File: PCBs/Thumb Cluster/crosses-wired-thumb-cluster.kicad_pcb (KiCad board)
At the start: 2 copper layers, 126.8 x 111 mm, 46 parts, among them J1 SM06B-SRSS-TB(LF)(SN), J2 SM06B-SRSS-TB(LF)(SN), J3 Conn_01x02_Socket, J4 Conn_01x14_Pin, J5 Conn_01x14_Pin, J6 Conn_01x02_Socket, P1 TYPE-C-31-M-12 USB, P2 TYPE-C-31-M-12 USB, U1 supermini nrf / nice nano v2, U2 supermini nrf / nice nano v2

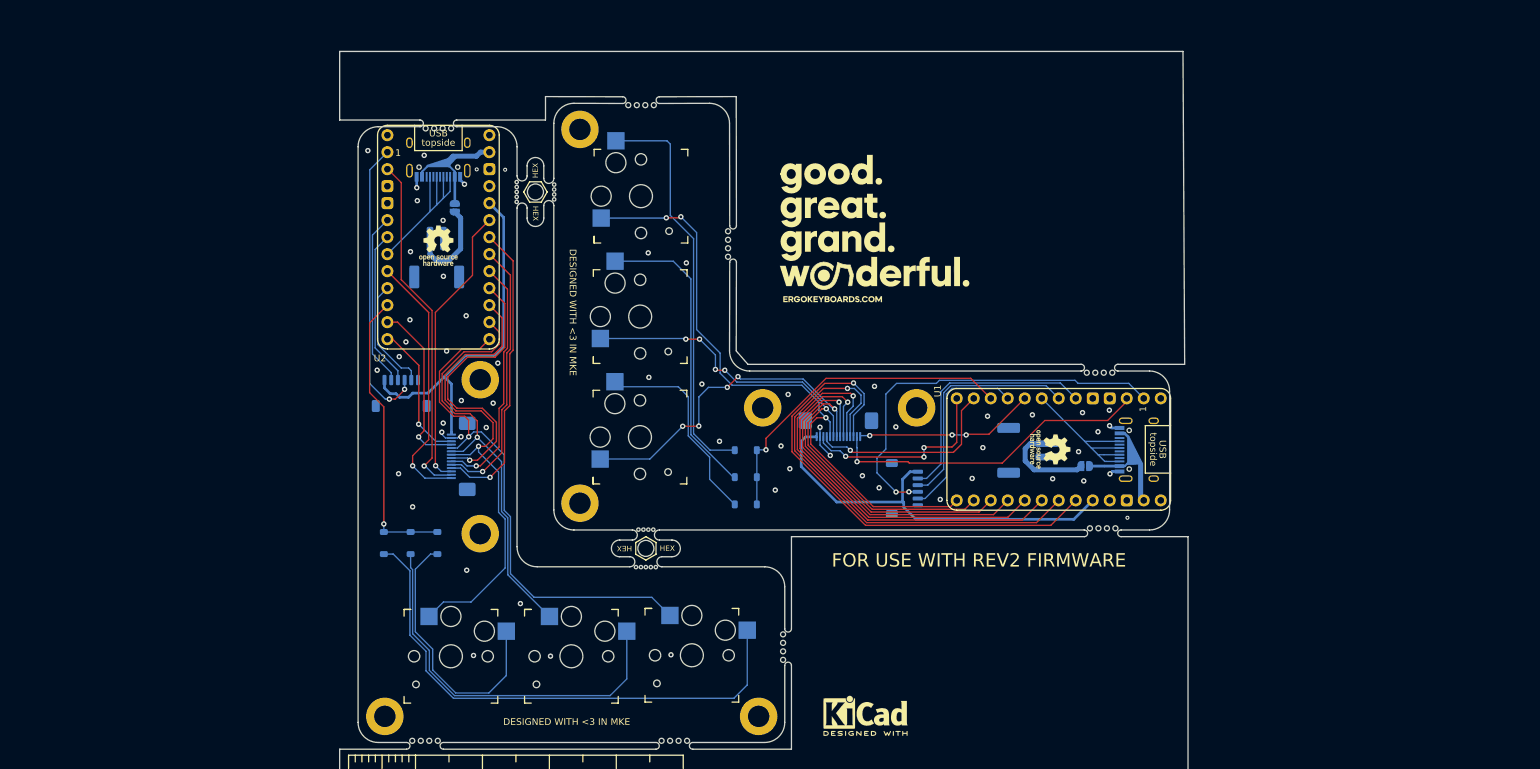
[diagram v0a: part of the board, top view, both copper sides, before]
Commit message: Added a project | Addded a Schematic | Started the board routing
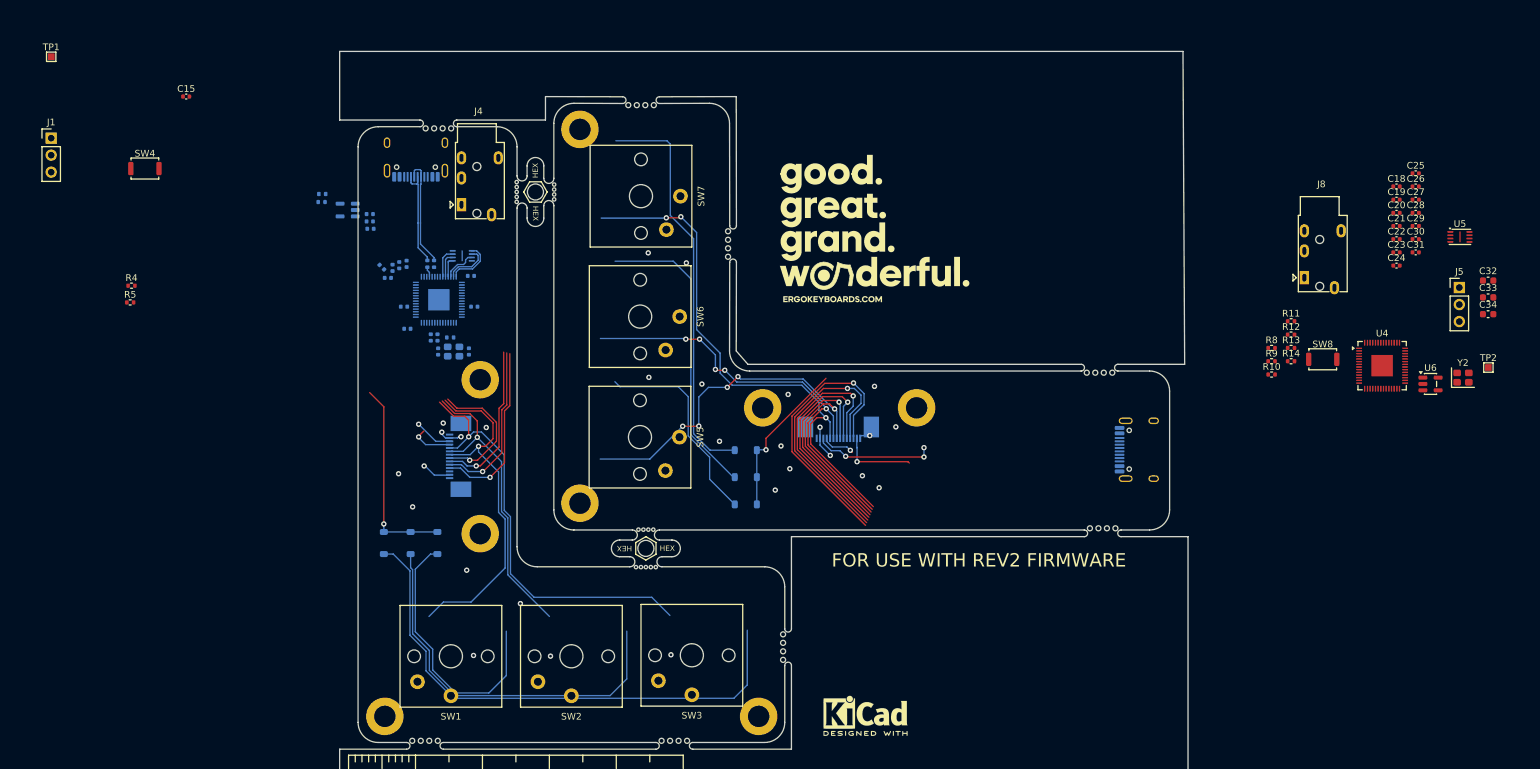
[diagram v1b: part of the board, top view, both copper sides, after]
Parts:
- removed the J2 at (106.7, 147.6)
- removed the J3 at (200.3, 156.1)
- removed the J6 at (112.0, 127.3)
- removed JP1, JP2: SolderJumper_2_Open, Jumper:SolderJumper-2_P1.3mm_Open_RoundedPad1.0x1.5mm
- removed the REF** at (112.2, 125.5)
- removed the REF** at (203.7, 156.0)
- added C1: 15pF, Capacitor_SMD:C_0402_1005Metric, B.Cu at (116.8, 141.3)
- added C10: 0.1uF, Capacitor_SMD:C_0402_1005Metric, B.Cu at (105.4, 128.8)
- added C11: 0.1uF, Capacitor_SMD:C_0402_1005Metric, B.Cu at (104.7, 130.3)
- added C12: 0.1uF, Capacitor_SMD:C_0402_1005Metric, B.Cu at (117.1, 130.0)
- added C13: 0.1uF, Capacitor_SMD:C_0402_1005Metric, B.Cu at (111.1, 139.2)
- added C14: 0.1uF, Capacitor_SMD:C_0402_1005Metric, B.Cu at (107.5, 128.2)
- added C15: 1uF, Capacitor_SMD:C_0402_1005Metric, F.Cu at (74.6, 103.2)
- added C16: 1uF, Capacitor_SMD:C_0402_1005Metric, B.Cu at (102.0, 120.8)
- added C17: 1uF, Capacitor_SMD:C_0402_1005Metric, B.Cu at (102.0, 121.9)
- added C18: 15pF, Capacitor_SMD:C_0402_1005Metric, F.Cu at (255.4, 116.7)
- added C19: 1uF, Capacitor_SMD:C_0402_1005Metric, F.Cu at (255.4, 118.7)
- added C2: 1uF, Capacitor_SMD:C_0402_1005Metric, B.Cu at (102.1, 123.0)
- added C20: 1uF, Capacitor_SMD:C_0402_1005Metric, F.Cu at (255.4, 120.6)
- added C21: 15pF, Capacitor_SMD:C_0402_1005Metric, F.Cu at (255.4, 122.6)
- added C22: 0.1uF, Capacitor_SMD:C_0402_1005Metric, F.Cu at (255.4, 124.6)
- added C23: 0.1uF, Capacitor_SMD:C_0402_1005Metric, F.Cu at (255.4, 126.5)
- added C24: 0.1uF, Capacitor_SMD:C_0402_1005Metric, F.Cu at (255.4, 128.5)
- added C25: 0.1uF, Capacitor_SMD:C_0402_1005Metric, F.Cu at (258.3, 114.7)
- added C26: 0.1uF, Capacitor_SMD:C_0402_1005Metric, F.Cu at (258.3, 116.7)
- added C27: 0.1uF, Capacitor_SMD:C_0402_1005Metric, F.Cu at (258.3, 118.7)
- added C28: 0.1uF, Capacitor_SMD:C_0402_1005Metric, F.Cu at (258.3, 120.6)
- added C29: 0.1uF, Capacitor_SMD:C_0402_1005Metric, F.Cu at (258.3, 122.6)
- added C3: 1uF, Capacitor_SMD:C_0402_1005Metric, B.Cu at (107.6, 137.9)
- added C30: 0.1uF, Capacitor_SMD:C_0402_1005Metric, F.Cu at (258.3, 124.6)
- added C31: 0.1uF, Capacitor_SMD:C_0402_1005Metric, F.Cu at (258.3, 126.5)
- added C32: 1uF, Capacitor_SMD:C_0603_1608Metric, F.Cu at (269.1, 130.7)
- added C33: 1uF, Capacitor_SMD:C_0603_1608Metric, F.Cu at (269.1, 133.2)
- added C34: 1uF, Capacitor_SMD:C_0603_1608Metric, F.Cu at (269.1, 135.8)
- added C4: 15pF, Capacitor_SMD:C_0402_1005Metric, B.Cu at (112.2, 141.3)
- added C5: 0.1uF, Capacitor_SMD:C_0402_1005Metric, B.Cu at (117.6, 134.6)
- added C6: 0.1uF, Capacitor_SMD:C_0402_1005Metric, B.Cu at (107.1, 134.6)
- added C7: 0.1uF, Capacitor_SMD:C_0402_1005Metric, B.Cu at (103.8, 128.7)
- added C8: 0.1uF, Capacitor_SMD:C_0402_1005Metric, B.Cu at (112.1, 139.2)
- added C9: 0.1uF, Capacitor_SMD:C_0402_1005Metric, B.Cu at (106.4, 128.4)
- added J4: AudioJack4, Connector_Audio:Jack_3.5mm_PJ320E_Horizontal, F.Cu at (115.7, 119.4)
- added J5: Conn_01x03, Connector_PinHeader_2.54mm:PinHeader_1x03_P2.54mm_Vertical, F.Cu at (264.8, 131.8)
- added J8: AudioJack4, Connector_Audio:Jack_3.5mm_PJ320E_Horizontal, F.Cu at (241.6, 130.3)
- added R1: 1K, Resistor_SMD:R_0402_1005Metric, B.Cu at (114.0, 139.2)
- added R10: 27, Resistor_SMD:R_0402_1005Metric, F.Cu at (236.7, 144.8)
- added R11: 1K, Resistor_SMD:R_0402_1005Metric, F.Cu at (239.7, 136.8)
- added R12: 10K, Resistor_SMD:R_0402_1005Metric, F.Cu at (239.7, 138.8)
- added R13: 5.1K, Resistor_SMD:R_0402_1005Metric, F.Cu at (239.7, 140.8)
- added R14: 5.1K, Resistor_SMD:R_0402_1005Metric, F.Cu at (239.7, 142.8)
- added R2: 27, Resistor_SMD:R_0402_1005Metric, B.Cu at (110.6, 128.2)
- added R3: 27, Resistor_SMD:R_0402_1005Metric, B.Cu at (111.6, 128.2)
- added R4: 1K, Resistor_SMD:R_0402_1005Metric, F.Cu at (66.4, 131.5)
- added R5: 10K, Resistor_SMD:R_0402_1005Metric, F.Cu at (66.2, 134.0)
- added R6: 5.1K, Resistor_SMD:R_0402_1005Metric, B.Cu at (94.9, 117.8)
- added R7: 5.1K, Resistor_SMD:R_0402_1005Metric, B.Cu at (94.8, 119.0)
- added R8: 1K, Resistor_SMD:R_0402_1005Metric, F.Cu at (236.7, 140.8)
- added R9: 27, Resistor_SMD:R_0402_1005Metric, F.Cu at (236.7, 142.8)
- added SW4: SW_Push, Button_Switch_SMD:SW_Push_SPST_NO_Alps_SKRK, F.Cu at (68.4, 114.0)
- added SW8: SW_Push, Button_Switch_SMD:SW_Push_SPST_NO_Alps_SKRK, F.Cu at (244.4, 142.5)
- added TP1: TestPoint, TestPoint:TestPoint_Pad_1.0x1.0mm, F.Cu at (54.4, 97.3)
- added TP2: TestPoint, TestPoint:TestPoint_Pad_1.0x1.0mm, F.Cu at (269.1, 143.7)
- added U3: XC6210B332MR, Package_TO_SOT_SMD:SOT-23-5, B.Cu at (98.7, 120.2)
- added U4: RP2040, Package_DFN_QFN:QFN-56-1EP_7x7mm_P0.4mm_EP3.2x3.2mm, F.Cu at (253.3, 143.4)
- added U5: W25Q128JVS, Package_SON:Winbond_USON-8-1EP_3x2mm_P0.5mm_EP0.2x1.6mm, F.Cu at (264.9, 124.2)
- added U6: XC6210B332MR, Package_TO_SOT_SMD:SOT-23-5, F.Cu at (260.5, 146.2)
- added Y1: Crystal_GND24, Crystal:Crystal_SMD_2520-4Pin_2.5x2.0mm, B.Cu at (114.5, 141.3)
- added Y2: Crystal_GND24, Crystal:Crystal_SMD_2520-4Pin_2.5x2.0mm, F.Cu at (265.3, 145.2)
- D1: renamed from D6; value 1N4148 -> D
- D2: renamed from D5; value 1N4148 -> D
- D3: renamed from D4; value 1N4148 -> D
- D4: renamed from D1; value 1N4148 -> D
- D5: renamed from D2; value 1N4148 -> D
- D6: renamed from D3; value 1N4148 -> D
- J1: value SM06B-SRSS-TB(LF)(SN) -> Conn_01x03; footprint Connector_JST:JST_SH_SM06B-SRSS-TB_1x06-1MP_P1.00mm_Horizontal -> Connector_PinHeader_2.54mm:PinHeader_1x03_P2.54mm_Vertical; moved to F.Cu
- J2: renamed from P2; value TYPE-C-31-M-12 USB -> USB_C_Receptacle_USB2.0_16P; footprint PCM_marbastlib-various:USB_C_Receptacle_HRO_TYPE-C-31-M-12 -> Connector_USB:USB_C_Receptacle_HRO_TYPE-C-31-M-12
- J3: renamed from J5; footprint PCM_marbastlib-various:XUNPU_FPC-05F-14PH20_1x14-1MP_P0.5mm_Horizontal -> Connector_FFC-FPC:TE_1-1734839-4_1x14-1MP_P0.5mm_Horizontal
- J6: renamed from P1; value TYPE-C-31-M-12 USB -> USB_C_Receptacle_USB2.0_16P; footprint PCM_marbastlib-various:USB_C_Receptacle_HRO_TYPE-C-31-M-12 -> Connector_USB:USB_C_Receptacle_HRO_TYPE-C-31-M-12
- J7: renamed from J4; footprint PCM_marbastlib-various:XUNPU_FPC-05F-14PH20_1x14-1MP_P0.5mm_Horizontal -> Connector_FFC-FPC:TE_1-1734839-4_1x14-1MP_P0.5mm_Horizontal
- SW1: renamed from CH6; value CPG135001S30 -> SW_Push; footprint keyswitches:Kailh_socket_PG1350 -> PCM_Switch_Keyboard_Kailh:SW_Kailh_Choc_V1_1.00u
- SW2: renamed from CH5; value CPG135001S30 -> SW_Push; footprint keyswitches:Kailh_socket_PG1350 -> PCM_Switch_Keyboard_Kailh:SW_Kailh_Choc_V1_1.00u
- SW3: renamed from CH4; value CPG135001S30 -> SW_Push; footprint keyswitches:Kailh_socket_PG1350 -> PCM_Switch_Keyboard_Kailh:SW_Kailh_Choc_V1_1.00u
- SW5: renamed from CH3; value CPG135001S30 -> SW_Push; footprint keyswitches:Kailh_socket_PG1350 -> PCM_Switch_Keyboard_Kailh:SW_Kailh_Choc_V1_1.00u
- SW6: renamed from CH2; value CPG135001S30 -> SW_Push; footprint keyswitches:Kailh_socket_PG1350 -> PCM_Switch_Keyboard_Kailh:SW_Kailh_Choc_V1_1.00u
- SW7: renamed from CH1; value CPG135001S30 -> SW_Push; footprint keyswitches:Kailh_socket_PG1350 -> PCM_Switch_Keyboard_Kailh:SW_Kailh_Choc_V1_1.00u
- U1: value supermini nrf / nice nano v2 -> RP2040; footprint PCM_marbastlib-xp-promicroish:Helios_AH_USBup -> Package_DFN_QFN:QFN-56-1EP_7x7mm_P0.4mm_EP3.2x3.2mm; moved to B.Cu
- U2: value supermini nrf / nice nano v2 -> W25Q128JVS; footprint PCM_marbastlib-xp-promicroish:Helios_AH_USBup -> Package_SON:Winbond_USON-8-1EP_3x2mm_P0.5mm_EP0.2x1.6mm; moved to B.Cu
- moved J1 137.8 mm to (54.4, 109.5), turned to 0 degrees
- moved U1 94.1 mm to (112.3, 133.6), turned to 180 degrees
- moved U2 3.87 mm to (115.8, 127.0), turned to 180 degrees
- moved J2 3.35 mm to (108.9, 111.2)
- renumbered H3 to H1, H3 to H2, H2 to H3, H1 to H4, H3 to H5, H3 to H6, H2 to H7, H1 to H8
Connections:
- D1 pad 1: R-ROW3 -> /R-ROW3
- D2 pad 1: R-ROW3 -> /R-ROW3
- D3 pad 1: R-ROW3 -> /R-ROW3
- D4 pad 1: L-ROW3 -> /L-ROW3
- D4 pad 2: Net-(D1-A) (its old number) -> Net-(D4-A)
- D5 pad 1: L-ROW3 -> /L-ROW3
- D6 pad 1: L-ROW3 -> /L-ROW3
- D6 pad 2: Net-(D3-A) (its old number) -> Net-(D6-A)
- J1 pad 1: GND -> /R-SWCLK
- J1 pad 2: L-CS -> GND-R
- J1 pad 3: L-MISO -> /R-SWDI0
- J2 pad A1: GND -> GND-R
- J2 pad A12: GND -> GND-R
- J2 pad A4: VBATTR -> VBUS-R
- J2 pad A5: R-DATA -> Net-(J2-CC1)
- J2 pad A6: R-DATA -> /R-USB_DP
- J2 pad A7: unconnected-(P2-D--PadA7) -> /R-USB_DN
- J2 pad A8: (no net) -> unconnected-(J2-SBU1-PadA8)
- J2 pad A9: VBATTR -> VBUS-R
- J2 pad B1: GND -> GND-R
- J2 pad B12: GND -> GND-R
- J2 pad B4: VBATTR -> VBUS-R
- J2 pad B5: R-DATA -> Net-(J2-CC2)
- J2 pad B6: R-DATA -> /R-USB_DP
- J2 pad B7: unconnected-(P2-D--PadB7) -> /R-USB_DN
- J2 pad B8: (no net) -> unconnected-(J2-SBU2-PadB8)
- J2 pad B9: VBATTR -> VBUS-R
- J3 pad 1: R-VCC -> unconnected-(J3-Pin_1-Pad1)
- J3 pad 10: R-ROW0 -> /R-ROW0
- J3 pad 11: R-ROW1 -> /R-ROW1
- J3 pad 12: R-ROW2 -> /R-ROW2
- J3 pad 13: R-COLP -> /R-COLP
- J3 pad 14: R-ROWH -> /R-ROWH
- J3 pad 2: GND -> GND-R
- J3 pad 3: R-I2C SCL -> unconnected-(J3-Pin_3-Pad3)
- J3 pad 4: R-I2C SDA -> unconnected-(J3-Pin_4-Pad4)
- J3 pad 5: R-COL2 -> /R-COL2
- J3 pad 6: R-COL3 -> /R-COL3
- J3 pad 7: R-COL4 -> /R-COL4
- J3 pad 8: R-COL1 -> /R-COL1
- J3 pad 9: R-COL0 -> /R-COL0
- J6 pad A1: GND -> GND-L
- J6 pad A12: GND -> GND-L
- J6 pad A4: VBATTL -> VBUS-L
- J6 pad A5: L-DATA -> Net-(J6-CC1)
- J6 pad A6: L-DATA -> /L-USB_DP
- J6 pad A7: unconnected-(P1-D--PadA7) -> /L-USB_DM
- J6 pad A8: (no net) -> unconnected-(J6-SBU1-PadA8)
- J6 pad A9: VBATTL -> VBUS-L
- J6 pad B1: GND -> GND-L
- J6 pad B12: GND -> GND-L
- J6 pad B4: VBATTL -> VBUS-L
- J6 pad B5: L-DATA -> Net-(J6-CC2)
- J6 pad B6: L-DATA -> /L-USB_DP
- J6 pad B7: unconnected-(P1-D--PadB7) -> /L-USB_DM
- J6 pad B8: (no net) -> unconnected-(J6-SBU2-PadB8)
- J6 pad B9: VBATTL -> VBUS-L
- J7 pad 1: L-VCC -> unconnected-(J7-Pin_1-Pad1)
- J7 pad 10: L-ROW0 -> /L-ROW0
- J7 pad 11: L-ROW1 -> /L-ROW1
- J7 pad 12: L-ROW2 -> /L-ROW2
- J7 pad 13: L-COLP -> /L-COLP
- J7 pad 14: L-ROWH -> /L-ROWH
- J7 pad 2: GND -> GND-L
- J7 pad 3: L-I2C SCL -> unconnected-(J7-Pin_3-Pad3)
- J7 pad 4: L-I2C SDA -> unconnected-(J7-Pin_4-Pad4)
- J7 pad 5: L-COL2 -> /L-COL2
- J7 pad 6: L-COL3 -> /L-COL3
- J7 pad 7: L-COL4 -> /L-COL4
- J7 pad 8: L-COL1 -> /L-COL1
- J7 pad 9: L-COL0 -> /L-COL0
- SW1 pad 1: R-COL4 -> /R-COL4
- SW2 pad 1: R-COL3 -> /R-COL3
- SW3 pad 1: R-COL2 -> /R-COL2
- SW5 pad 1: L-COL4 -> /L-COL4
- SW5 pad 2: Net-(D3-A) (its old number) -> Net-(D4-A)
- SW6 pad 1: L-COL3 -> /L-COL3
- SW7 pad 1: L-COL2 -> /L-COL2
- SW7 pad 2: Net-(D1-A) (its old number) -> Net-(D6-A)
- U1 pad 1: L-MISO -> +3V3-R
- U1 pad 10: L-ROW3 -> +3V3-R
- U1 pad 11: L-I2C SDA -> unconnected-(U1-GPIO8-Pad11)
- U1 pad 12: L-I2C SCL -> unconnected-(U1-GPIO9-Pad12)
- U1 pad 13: VBATTL -> unconnected-(U1-GPIO10-Pad13)
- U1 pad 14: GND -> unconnected-(U1-GPIO11-Pad14)
- U1 pad 16: L-VCC -> unconnected-(U1-GPIO13-Pad16)
- U1 pad 17: L-ROW2 -> unconnected-(U1-GPIO14-Pad17)
- U1 pad 18: L-ROW1 -> unconnected-(U1-GPIO15-Pad18)
- U1 pad 19: L-ROW0 -> GND-R
- U1 pad 2: L-COLP -> unconnected-(U1-GPIO0-Pad2)
- U1 pad 20: L-COL0 -> Net-(U1-XIN)
- U1 pad 21: L-COL1 -> Net-(U1-XOUT)
- U1 pad 22: L-COL4 -> +3V3-R
- U1 pad 23: L-COL3 -> +1V1-R
- U1 pad 24: L-COL2 -> /R-SWCLK
- U1 pad 3: GND -> unconnected-(U1-GPIO1-Pad3)
- U1 pad 31: (no net) -> unconnected-(U1-GPIO20-Pad31)
- U1 pad 4: GND -> unconnected-(U1-GPIO2-Pad4)
- U1 pad 5: L-SCK -> unconnected-(U1-GPIO3-Pad5)
- U1 pad 6: L-MOSI -> unconnected-(U1-GPIO4-Pad6)
- U1 pad 7: L-DATA -> unconnected-(U1-GPIO5-Pad7)
- U1 pad 8: L-ROWH -> unconnected-(U1-GPIO6-Pad8)
- U1 pad 9: L-CS -> unconnected-(U1-GPIO7-Pad9)
- U2 pad 1: R-MISO -> /R-QSPI_SS
- U2 pad 2: R-COLP -> /R-QSPI_SD1
- U2 pad 3: GND -> /R-QSPI_SD2
- U2 pad 4: GND -> GND-R
- U2 pad 5: R-SCK -> /R-QSPI_SD0
- U2 pad 6: R-MOSI -> /R-QSPI_SCLK
- U2 pad 7: R-DATA -> /R-QSPI_SD3
- U2 pad 8: R-ROWH -> +3V3-R
- U2 pad 9: R-CS -> (no net)
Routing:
- net Net-(D4-A): track 0.00 -> 139.8 mm
- net L-COL2: track 91.9 -> 0.00 mm, vias 3 -> 0
- net L-COL4: track 90.9 -> 0.00 mm, vias 5 -> 0
- net L-COL3: track 80.4 -> 0.00 mm, vias 5 -> 0
- net Net-(D3-A): track 79.6 -> 0.00 mm
- net /L-COL2: track 0.00 -> 79.0 mm, vias 0 -> 3
- net R-COL2: track 76.9 -> 0.00 mm, vias 1 -> 0
- net L-ROW2: track 74.4 -> 0.00 mm, vias 1 -> 0
- net R-COL4: track 73.3 -> 0.00 mm, vias 1 -> 0
- net /L-COL4: track 0.00 -> 72.3 mm, vias 0 -> 5
- net Net-(D6-A): track 0.00 -> 71.3 mm
- net L-ROW1: track 69.3 -> 0.00 mm, vias 1 -> 0
- net /L-COL3: track 0.00 -> 64.7 mm, vias 0 -> 5
- net L-ROW0: track 63.3 -> 0.00 mm, vias 1 -> 0
- net R-COL3: track 63.3 -> 0.00 mm, vias 1 -> 0
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- added copper zone on B.Cu, net GND-L
- added copper zone on F.Cu, net GND-L
- removed copper zone on B.Cu, net GND
- removed copper zone on F.Cu, net GND
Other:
- copper layers 2 -> 4
- board text removed: "CROSSES REV12"
- board text removed: "DESIGNED WITH <3 IN MKE"

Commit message: Finished routing right side thumb cluster
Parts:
- removed REF** (x8): mousebites 1mm, PCM_marbastlib-various:mousebites_1mm
- removed REF**: KiCad-Logo2_5mm_SilkScreen, Symbol:KiCad-Logo2_5mm_SilkScreen
- removed REF**: Gauge_50mm_Type1_SilkScreenTop, Calibration_Scale:Gauge_50mm_Type1_SilkScreenTop
- C15, R4, R5, TP1: moved to B.Cu
- C2, C3: footprint Capacitor_SMD:C_0402_1005Metric -> Capacitor_SMD:C_0603_1608Metric
- moved TP1 165.3 mm to (214.3, 139.4)
- moved SW4 164.5 mm to (232.7, 122.4), turned to -90 degrees
- moved R5 164.1 mm to (230.2, 127.7), turned to 90 degrees
- moved R4 163.9 mm to (230.2, 125.7), turned to -90 degrees
- moved J1 163.7 mm to (213.5, 148.1), turned to 180 degrees
- moved C15 152.9 mm to (225.8, 125.8)
- moved R7 133.3 mm to (228.1, 117.5), turned to 90 degrees
- moved R6 130.2 mm to (225.1, 117.5), turned to -90 degrees
- moved U3 124.3 mm to (223.0, 120.5), turned to -90 degrees
- moved C17 119.5 mm to (221.5, 123.2)
- moved C16 118.8 mm to (220.8, 120.6), turned to -90 degrees
- moved J2 117.5 mm to (226.4, 111.2)
- moved C2 114.4 mm to (216.4, 128.9), turned to 90 degrees
- moved C7 114.1 mm to (217.9, 127.4)
- moved C11 113.3 mm to (218.0, 130.9)
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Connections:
- R2 pad 2: Net-(U1-USB_DM) -> /R-USB_DN
- R3 pad 1: Net-(U1-USB_DP) -> /R-USB_DP
- U1 pad 12: unconnected-(U1-GPIO9-Pad12) -> /R-ROW1
- U1 pad 13: unconnected-(U1-GPIO10-Pad13) -> /R-ROW0
- U1 pad 14: unconnected-(U1-GPIO11-Pad14) -> /R-COL0
- U1 pad 15: unconnected-(U1-GPIO12-Pad15) -> /R-COL1
- U1 pad 16: unconnected-(U1-GPIO13-Pad16) -> /R-COL4
- U1 pad 17: unconnected-(U1-GPIO14-Pad17) -> /R-COL3
- U1 pad 18: unconnected-(U1-GPIO15-Pad18) -> /R-COL2
- U1 pad 28: unconnected-(U1-GPIO17-Pad28) -> /R-ROW2
- U1 pad 29: unconnected-(U1-GPIO18-Pad29) -> /R-COLP
- U1 pad 30: unconnected-(U1-GPIO19-Pad30) -> /R-ROWH
- U1 pad 31: unconnected-(U1-GPIO20-Pad31) -> /R-ROW3
- U1 pad 41: unconnected-(U1-GPIO29/ADC3-Pad41) -> /R-SERIAL
- U1 pad 46: Net-(U1-USB_DM) -> /R-USB_DN
- U1 pad 47: Net-(U1-USB_DP) -> /R-USB_DP
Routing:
- net Net-(D4-A): track 139.8 -> 0.00 mm
- net Net-(D5-A): track 102.7 -> 0.00 mm
- net Net-(D6-A): track 71.3 -> 0.00 mm
- net +3V3-R: track 0.00 -> 52.7 mm, vias 0 -> 2
- net Net-(D3-A): track 0.00 -> 52.2 mm, vias 0 -> 2
- net /L-COL4: track 72.3 -> 20.4 mm, vias 5 -> 0
- net GND-R: track 3.94 -> 49.6 mm, vias 2 -> 26
- net /L-COL2: track 79.0 -> 38.8 mm, vias 3 -> 1
- net Net-(D2-A): track 0.00 -> 32.1 mm, vias 0 -> 2
- net /R-ROWH: track 0.00 -> 31.4 mm, vias 0 -> 2
- net /R-ROW2: track 0.00 -> 28.9 mm, vias 0 -> 2
- net /R-COL3: track 44.9 -> 72.9 mm, vias 1 -> 2
- net /R-SERIAL: track 0.00 -> 27.9 mm
- net /R-COL2: track 62.8 -> 90.6 mm, vias 1 -> 2
- net /R-COL4: track 52.3 -> 78.9 mm, vias 1 -> 2
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- added copper zone on B.Cu, net +3V3-R
- added copper zone on B.Cu, net GND-R
- added copper zone on F.Cu, net GND-R
- removed copper zone on B.Cu, net GND-L
- removed copper zone on F.Cu, net GND-L
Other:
- board size 126.8 x 111 mm -> 133 x 92 mm
- copper layers 4 -> 2
- board text removed: "FOR USE WITH REV2 FIRMWARE"
